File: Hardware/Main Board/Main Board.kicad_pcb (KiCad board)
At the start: 2 copper layers, 78.7 x 29.1 mm, 55 parts, among them Q1 MMBT3904-TP, Q2 MMBT3904-TP, Q3 AO4484, SW1 Momentary, U1 MT3608, U2 NCP718A, U3 ATtiny1614, U4 TP4056

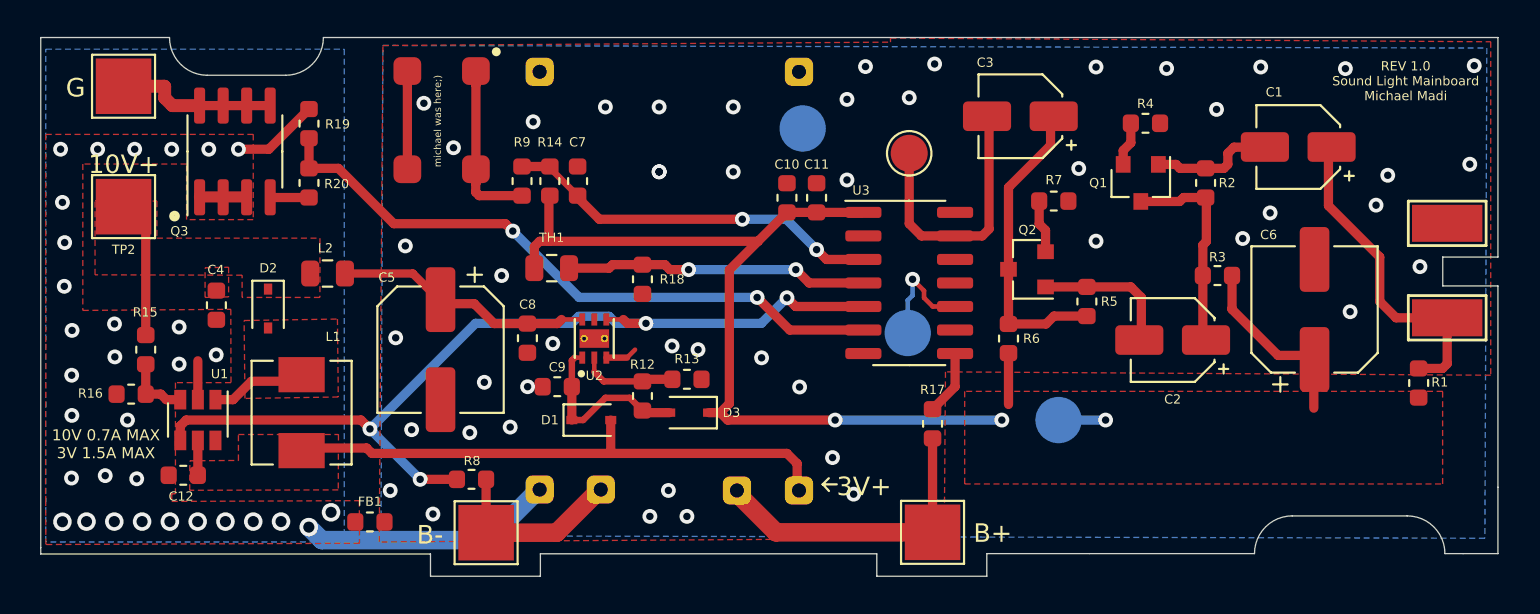
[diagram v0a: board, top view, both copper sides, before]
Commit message: board sent for production
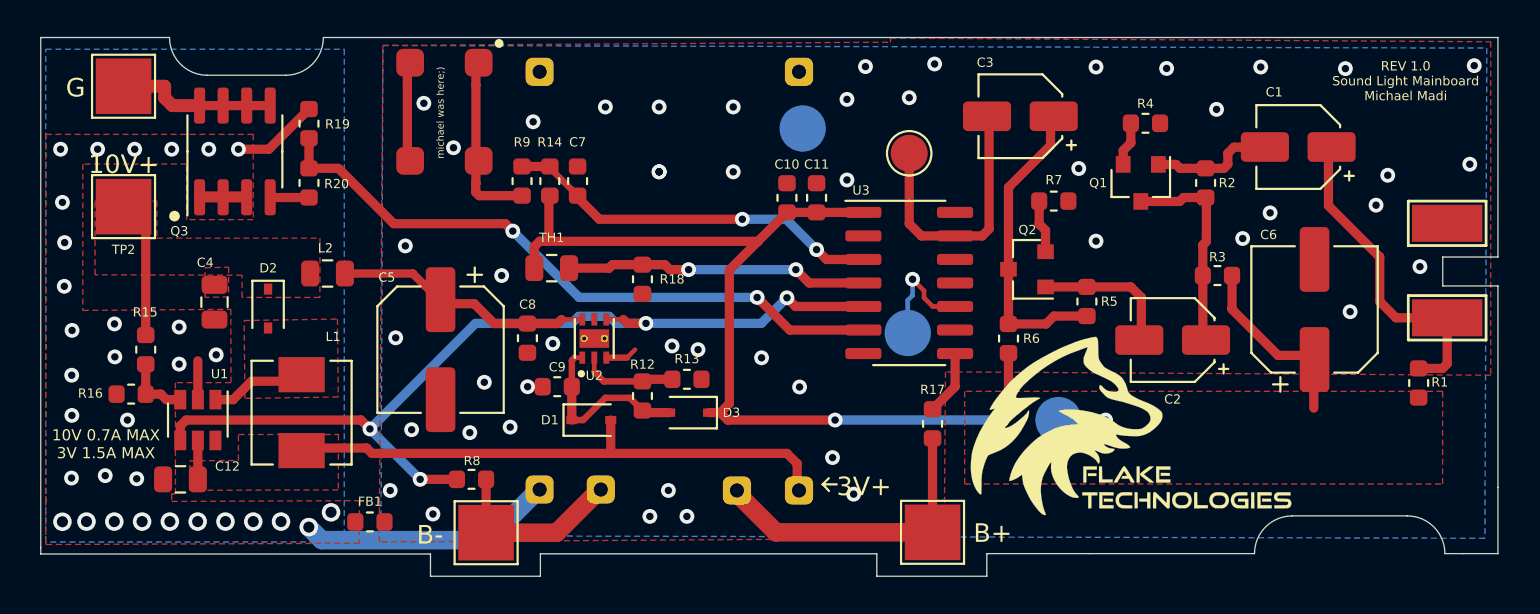
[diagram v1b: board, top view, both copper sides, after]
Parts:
- added G***: LOGO, Main Board1:FlakeTechnologies, F.Cu at (166.4, 105.2)
- added G***: LOGO, Main Board1:DDR, B.Cu at (139.7, 93.7)
- added G***: LOGO, Main Board1:3333, B.Cu at (180.1, 101.8)
- C12, C4: footprint Capacitor_SMD:C_0603_1608Metric -> Capacitor_SMD:C_0805_2012Metric
- moved C12 0.27 mm to (114.7, 107.6)
- moved C4 0.19 mm to (116.5, 98.0)
